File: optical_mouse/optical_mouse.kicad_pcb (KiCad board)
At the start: 2 copper layers, 12 parts, among them X1 CRYSTAL

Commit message: first viable layout
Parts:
- removed X1: CRYSTAL, 3PIN_6mm
- added ??1: ANDS-2610, adns-2610-DIP-8, F.Cu at (190.5, 171.4)
- added Q1: CSTLS_G, murata-resonators-CSTLS_G8, F.Cu at (186.7, 175.3)
- added U1: ARDUINO_MINI, arduino_mini, F.Cu at (167.6, 168.9)
- R1, R2, R3, R4: footprint R3-5 -> R4
- moved R4 157.1 mm to (191.8, 184.2), turned to 180 degrees
- moved R3 149.4 mm to (191.8, 181.6), turned to 180 degrees
- moved R1 143.8 mm to (190.5, 152.4), turned to 180 degrees
- moved C1 139.2 mm to (196.8, 174.0), turned to 90 degrees
- moved R2 135.6 mm to (190.5, 149.9), turned to 180 degrees
- moved D2 129.6 mm to (191.8, 157.5), turned to 180 degrees
- moved D3 129.5 mm to (191.8, 175.3), turned to 180 degrees
- moved D4 128.8 mm to (180.3, 175.3), turned to 180 degrees
- moved D1 127.7 mm to (180.3, 157.5), turned to 180 degrees
- moved C3 120.7 mm to (196.8, 166.4), turned to 90 degrees
- moved C2 106.9 mm to (196.8, 160.0), turned to 270 degrees
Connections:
- D1 pad 1: +5V -> N-000009
- D1 pad 2: N-0000036 (its old number) -> N-000004
- D2 pad 1: +5V -> N-000001
- D2 pad 2: N-0000032 -> N-000002
- D3 pad 1: +5V -> N-0000011
- D3 pad 2: N-0000033 -> N-0000027
- D4 pad 1: +5V -> N-0000012
- D4 pad 2: N-0000034 -> N-0000025
- R1 pad 1: N-0000036 (its old number) -> +5V
- R1 pad 2: N-0000027 -> N-000009
- R2 pad 1: N-0000032 -> +5V
- R2 pad 2: N-0000026 -> N-000001
- R3 pad 1: N-0000033 -> +5V
- R3 pad 2: N-0000031 -> N-0000011
- R4 pad 1: N-0000034 -> +5V
- R4 pad 2: N-0000030 -> N-0000012
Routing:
- net +5V: track 0.00 -> 114.9 mm
- net GND: track 0.00 -> 95.0 mm
- net N-0000027: track 0.00 -> 26.8 mm
- net N-000002: track 0.00 -> 16.3 mm
- net N-000001: track 0.00 -> 15.2 mm
- net N-0000012: track 0.00 -> 14.0 mm
- net N-0000032: track 0.00 -> 13.5 mm
- net N-0000011: track 0.00 -> 12.7 mm
- net N-0000033: track 0.00 -> 9.32 mm
- net N-0000025: track 0.00 -> 7.40 mm
- net N-000009: track 0.00 -> 6.66 mm
- net N-0000036: track 0.00 -> 5.61 mm
- net N-0000029: track 0.00 -> 4.70 mm
- net N-0000028: track 0.00 -> 4.60 mm
- net N-000004: track 0.00 -> 3.81 mm

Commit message: make room for mounting holes
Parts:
- moved C1 15.2 mm to (196.8, 158.8), turned to 270 degrees
- moved C2 12.7 mm to (196.8, 172.7), turned to 90 degrees
- moved R1 5.08 mm to (185.4, 152.4)
- moved R2 5.08 mm to (185.4, 149.9)
- moved R3 5.08 mm to (186.7, 181.6)
- moved R4 5.08 mm to (186.7, 184.2)
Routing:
- net GND: track 95.0 -> 106.4 mm
- net N-000001: track 15.2 -> 18.8 mm
- net +5V: track 114.9 -> 117.1 mm
- net N-0000012: track 14.0 -> 12.5 mm
- net N-0000011: track 12.7 -> 14.1 mm
- net N-000009: track 6.66 -> 5.61 mm
- net N-0000025: track 7.40 -> 6.66 mm
- net N-0000027: track 26.8 -> 26.0 mm
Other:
- board text added: "OptiMouseCam v 1.0 (C) Dave Berkeley 2015"

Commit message: more space for holes
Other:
- board outline added: 44.5 x 45.7 mm
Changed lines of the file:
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@@
     (links 26)
     (no_connects 0)
-    (area 158.378034 145.605499 199.710674 189.674501)
+    (area 157.429999 144.729999 201.980001 190.550001)
     (thickness 1.6)
-    (drawings 3)
+    (drawings 7)
     (tracks 98)
     (zones 0)
@@
     )
   )
+  (gr_line (start 157.48 190.5) (end 157.48 144.78) (angle 90) (layer Edge.Cuts) (width 0.1))
+  (gr_line (start 201.93 190.5) (end 157.48 190.5) (angle 90) (layer Edge.Cuts) (width 0.1))
+  (gr_line (start 201.93 144.78) (end 201.93 190.5) (angle 90) (layer Edge.Cuts) (width 0.1))
+  (gr_line (start 157.48 144.78) (end 201.93 144.78) (angle 90) (layer Edge.Cuts) (width 0.1))
   (gr_circle (center 186.0042 166.9542) (end 186.2582 167.1066) (layer B.SilkS) (width 0.2))
   (gr_circle (center 186.0296 166.9542) (end 188.1886 168.8084) (layer B.SilkS) (width 0.2))

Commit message: more messing with mounting holes
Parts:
- added 1PIN: P***, 1pin, F.Cu at (196.8, 185.4)
- added 1PIN: P***, 1pin, F.Cu at (196.8, 149.9)
- added 1PIN: P***, 1pin, F.Cu at (165.1, 149.9)
- added 1PIN: P***, 1pin, F.Cu at (165.1, 185.4)
- moved Q1 1.27 mm to (186.7, 176.5)
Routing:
- net N-0000027: track 26.0 -> 28.6 mm
- net N-0000032: track 13.5 -> 15.5 mm
- net N-0000033: track 9.32 -> 10.6 mm
- net N-0000011: track 14.1 -> 14.8 mm
- net GND: track 106.4 -> 105.9 mm

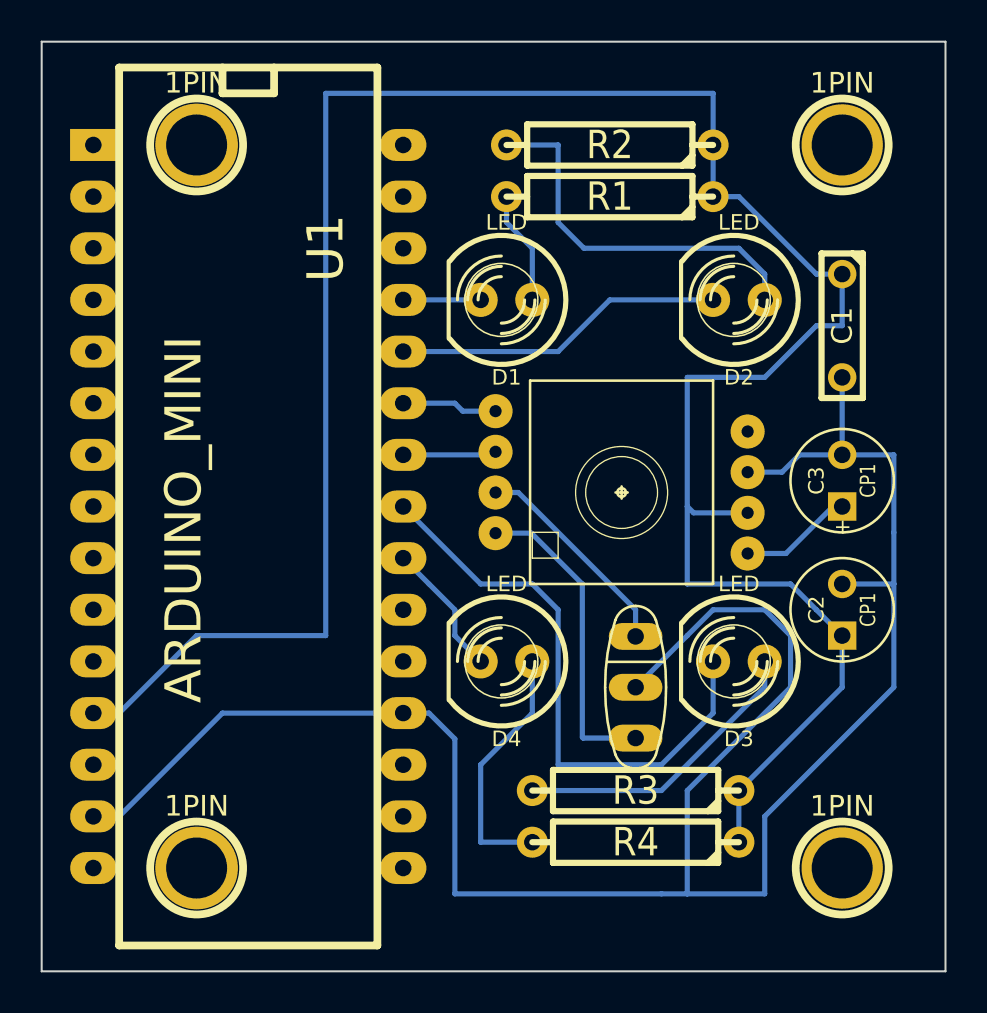
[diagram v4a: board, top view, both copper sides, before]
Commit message: added gnd plane
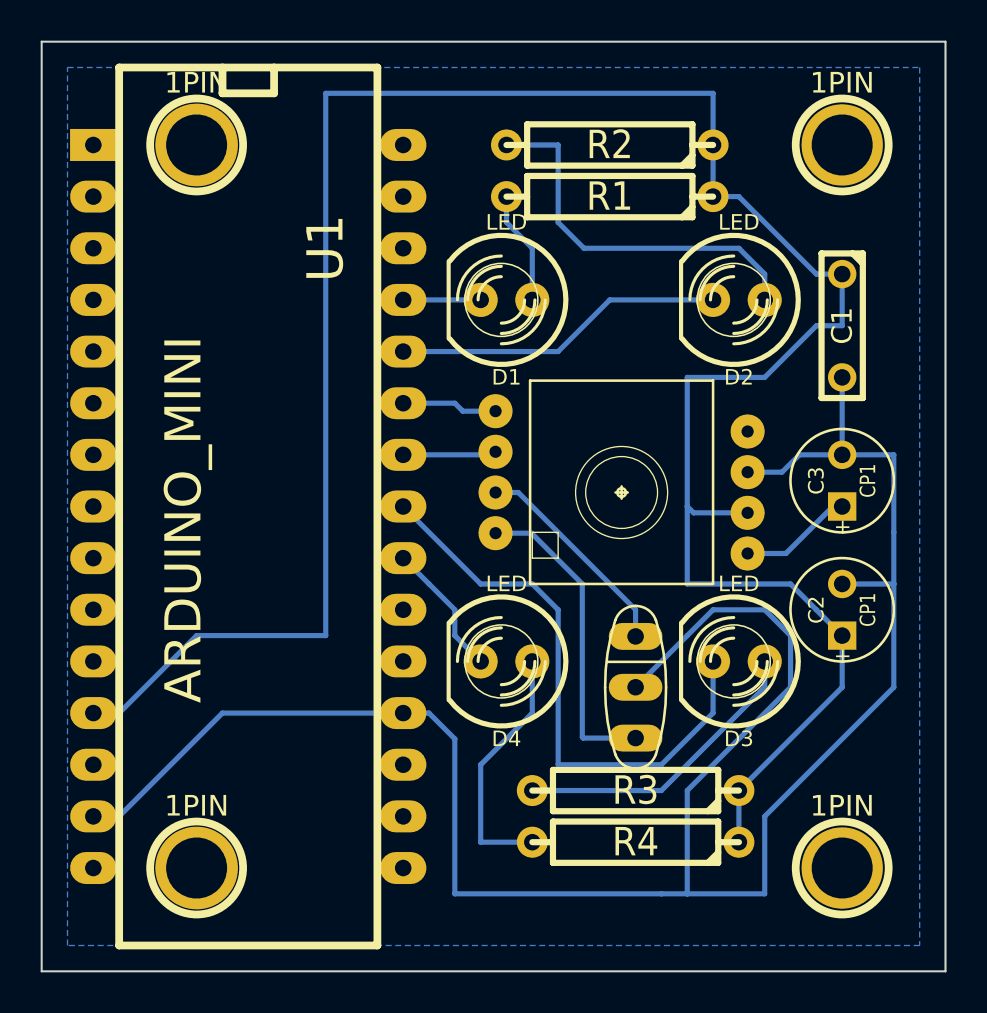
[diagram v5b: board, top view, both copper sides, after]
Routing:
- added copper zone on B.Cu, net GND
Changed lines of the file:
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@@
   (segment (start 181.61 154.94) (end 181.61 157.48) (width 0.254) (layer B.Cu) (net 15))
   (segment (start 180.34 153.67) (end 181.61 154.94) (width 0.254) (layer B.Cu) (net 15))
+  (zone (net 2) (net_name GND) (layer B.Cu) (hatch edge 0.508)
+    (connect_pads (clearance 0.508))
+    (min_thickness 0.254)
+    (fill (arc_segments 16) (thermal_gap 0.508) (thermal_bridge_width 0.508))
+    (polygon
+      (pts
+        (xy 200.66 189.23) (xy 158.75 189.23) (xy 158.75 146.05) (xy 200.66 146.05)
+      )
+    )
+  )
 )
